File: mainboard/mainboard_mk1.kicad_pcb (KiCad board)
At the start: 2 copper layers, 13 parts, among them J1 Conn_01x03_Pin, J2 Conn_01x03_Pin, J3 Conn_01x03_Pin, J4 Conn_01x03_Pin, J5 align2, J6 Conn_01x05_Pin, J7 Conn_01x02_Pin, J8 IMU, J9 align1, U1 74LS04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

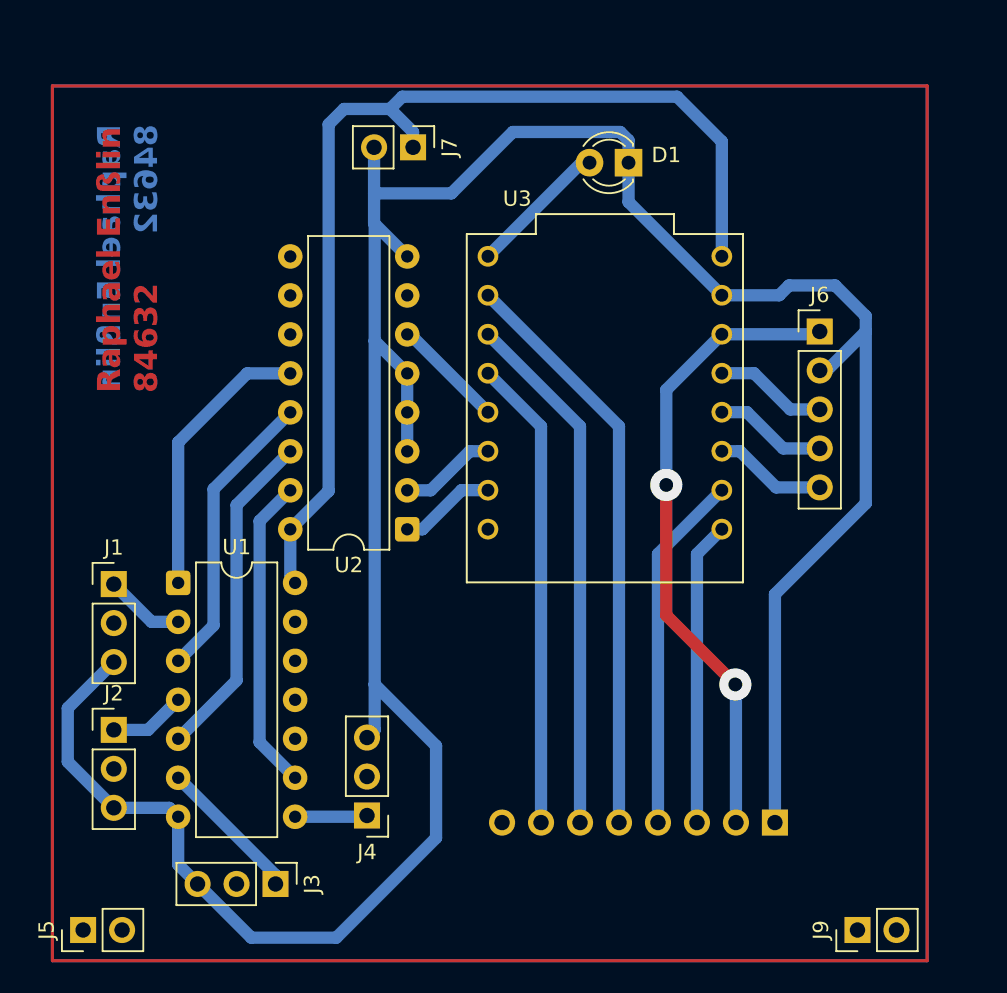
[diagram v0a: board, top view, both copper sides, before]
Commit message: mk1 3d view done
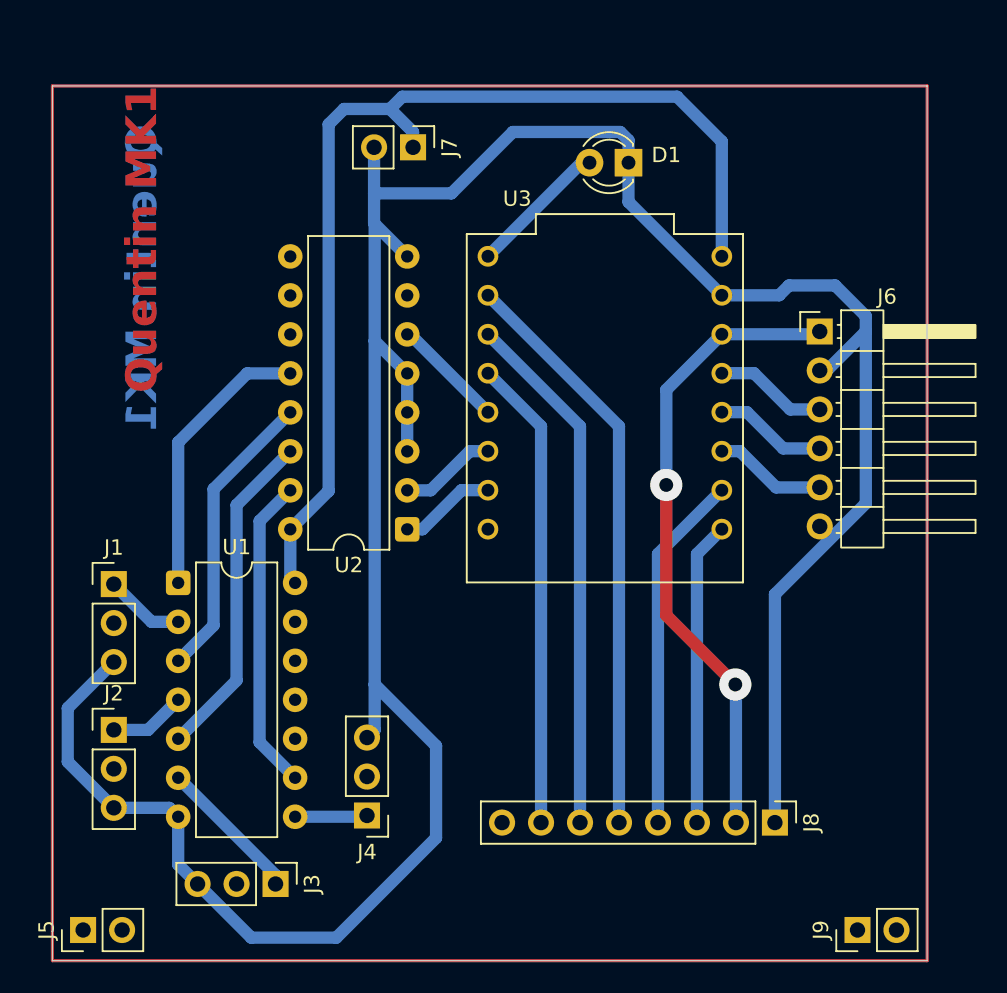
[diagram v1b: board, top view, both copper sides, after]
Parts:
- J6: footprint Connector_PinHeader_2.54mm:PinHeader_1x05_P2.54mm_Vertical -> Connector_PinHeader_2.54mm:PinHeader_1x06_P2.54mm_Horizontal
- J8: moved to F.Cu
- turned J8 to -90 degrees
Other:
- board outline added: 57 x 57 mm
- board text added: "Quentin MK1"
- board text removed: "Raphael Enßlin 84632"
